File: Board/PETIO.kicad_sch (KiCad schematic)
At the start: 63 parts, among them CN2 PORT_CASSETTE_EDGE, CN3 PORT_IEEE_EDGE, IC11 74138N, IC12 74145N, IC15 VIA, IC17 PIA, IC20 PIA, IC21 7417N, IC22 7400N, IC23 7486N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

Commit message: ultipet 1.1a board
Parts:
- removed R101, R34, R35, R86, R87: 4k7, cbm_ultipet_v1:0207_10, symbol cbm_ultipet_v1-eagle-import:R-EU_0207/10
- added IC48: 7414N, cbm_ultipet_v1:DIL14, symbol cbm_ultipet_v1-eagle-import:7414N
- added RN7: 4k7, cbm_ultipet_v1:RN-8, symbol cbm_ultipet_v1-eagle-import:RN07
- RN3, RN5: value 5k1 -> 2k4
- RN4, RN6: value 2k4 -> 5k1
- T6, T7: footprint cbm_ultipet_v1:TO92 -> Package_TO_SOT_THT:TO-92L_Inline_Wide
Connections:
- net BA2: now also IC48.1 (I)
- net C1MTR: now also RN7.3
- net C2MTR: now also RN7.4
- net OPENHIGH: now also RN7.2
- net VCC: now also RN7.1; no longer IC17.22 (CS0), IC20.22 (CS0)
- net VDRIVE: now also RN7.6
- net /SEL0: now reaches IC9.15 (Y0)
- net /SEL2 renamed /SEL2
- new net FUC1: RN7.5
- new net PULLUP_UART: RN7.7
- new net /BA2: IC17.22 (CS0), IC20.22 (CS0), IC48.2 (O)
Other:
- note added: "$e810-$e813"
- note added: "$e820-$e823"
- note added: "1.0B: - fix IEEE488 pull up/down resistor values (again) 1.1A: - fully decode PIA addresses - replace some discrete Rs with RN7 - fix 2N2222 footprint for new BOM part"
- note added: "CBM-ULTIPET-V1.1A"
- note added: "CBM-ULTIPET-V1.1A-20240616"
- note added: "To Pullups"
- note removed: "$e810-$e817 (2x)"
- note removed: "$e82x (4x)"
- note removed: "CBM-ULTIPET-V1.0A"
- note removed: "CBM-ULTIPET-V1.0A-20240104"
- moved on the sheet: RN3, RN5

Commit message: diverse fixes
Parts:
- removed JP15: JP1E, cbm_ultipet_v1:JP1, symbol cbm_ultipet_v1-eagle-import:JP1E
- removed JP8: JP2E, cbm_ultipet_v1:JP2, symbol cbm_ultipet_v1-eagle-import:JP2E
- added JP21: SolderJumper_3_Bridged12, Jumper:SolderJumper-3_P1.3mm_Bridged12_RoundedPad1.0x1.5mm_NumberLabels, symbol Jumper:SolderJumper_3_Bridged12
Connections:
- net BA7: now also IC9.4 (G2A); no longer IC11.4 (G2A)
- net GND: now also IC11.4 (G2A); no longer IC9.4 (G2A)
- net /LOCALIO: now also JP21.2 (C)
- net at IC11.15 (Y0): now also JP21.1 (A)
- net at IC11.7 (Y7): now also JP21.3 (B)
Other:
- note added: "1.0B: - fix IEEE488 pull up/down resistor values (again) 1.1A: - fully decode PIA addresses - replace some discrete Rs with RN7 - fix 2N2222 footprint for new BOM part 1.2A: - fix addressing 2nd SID by moving BA7 to IC9 - replace JP8 with a solder jumper (I/O block address)"
- note added: "CBM-ULTIPET-V1.2A"
- note added: "CBM-ULTIPET-V1.2A-20241010"
- note removed: "1.0B: - fix IEEE488 pull up/down resistor values (again) 1.1A: - fully decode PIA addresses - replace some discrete Rs with RN7 - fix 2N2222 footprint for new BOM part"
- note removed: "CBM-ULTIPET-V1.1A"
- note removed: "CBM-ULTIPET-V1.1A-20240616"

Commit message: various fixes as documented in github issues
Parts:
- D10: value 1N4148 -> 1N4448
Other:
- note added: "1.0B: - fix IEEE488 pull up/down resistor values (again) 1.1A: - fully decode PIA addresses - replace some discrete Rs with RN7 - fix 2N2222 footprint for new BOM part 1.2A: - fix addressing 2nd SID by moving BA7 to IC9 - replace JP8 with a solder jumper (I/O block address) - replace 1N4148 with 1N4448 for lower fwd voltage drop"
- note added: "CBM-ULTIPET-V1.2A-20241013"
- note removed: "1.0B: - fix IEEE488 pull up/down resistor values (again) 1.1A: - fully decode PIA addresses - replace some discrete Rs with RN7 - fix 2N2222 footprint for new BOM part 1.2A: - fix addressing 2nd SID by moving BA7 to IC9 - replace JP8 with a solder jumper (I/O block address)"
- note removed: "CBM-ULTIPET-V1.2A-20241010"
- moved on the sheet: D10
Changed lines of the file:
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@@
 	(wire
 		(pts
-			(xy 248.92 149.86) (xy 256.54 149.86)
+			(xy 248.92 153.67) (xy 256.54 153.67)
 		)
 		(stroke
@@
 	(wire
 		(pts
-			(xy 248.92 104.14) (xy 248.92 149.86)
+			(xy 248.92 104.14) (xy 248.92 153.67)
 		)
 		(stroke
@@
 	(wire
 		(pts
-			(xy 256.54 149.86) (xy 256.54 152.4)
+			(xy 256.54 153.67) (xy 256.54 157.48)
 		)
 		(stroke
@@
 	(wire
 		(pts
-			(xy 256.54 157.48) (xy 256.54 167.64)
+			(xy 256.54 162.56) (xy 256.54 167.64)
 		)
 		(stroke
@@
 		)
 	)
-	(text "1.0B: \n- fix IEEE488 pull up/down resistor values (again)\n1.1A:\n- fully decode PIA addresses\n- replace some discrete Rs with RN7\n- fix 2N2222 footprint for new BOM part\n1.2A:\n- fix addressing 2nd SID by moving BA7 to IC9\n- replace JP8 with a solder jumper (I/O block address)"
+	(text "1.0B: \n- fix IEEE488 pull up/down resistor values (again)\n1.1A:\n- fully decode PIA addresses\n- replace some discrete Rs with RN7\n- fix 2N2222 footprint for new BOM part\n1.2A:\n- fix addressing 2nd SID by moving BA7 to IC9\n- replace JP8 with a solder jumper (I/O block address)\n- replace 1N4148 with 1N4448 for lower fwd voltage drop"
 		(exclude_from_sim no)
-		(at 322.58 354.33 0)
+		(at 314.706 351.536 0)
 		(effects
 			(font
@@
 		)
 	)
-	(text "CBM-ULTIPET-V1.2A-20241010"
+	(text "CBM-ULTIPET-V1.2A-20241013\n"
 		(exclude_from_sim no)
 		(at 464.82 363.22 0)
@@
 	(global_label "/BIRQ"
 		(shape bidirectional)
-		(at 254 149.86 0)
+		(at 254 153.67 0)
 		(fields_autoplaced yes)
 		(effects
@@
 		)
 		(property "Intersheetrefs" "${INTERSHEET_REFS}"
-			(at 263.7039 149.86 0)
+			(at 263.7039 153.67 0)
 			(effects
 				(font
@@
 	(symbol
 		(lib_id "cbm_ultipet_v1-eagle-import:DIODE-D-5")
-		(at 256.54 154.94 270)
+		(at 256.54 160.02 270)
 		(unit 1)
 		(exclude_from_sim no)
@@
 		(dnp no)
 		(property "Reference" "D10"
-			(at 257.0226 157.48 0)
+			(at 257.0226 162.56 0)
 			(effects
 				(font
@@
 			)
 		)
-		(property "Value" "1N4148"
-			(at 254.2286 157.48 0)
+		(property "Value" "1N4448"
+			(at 254.2286 162.56 0)
 			(effects
 				(font
@@
 		)
 		(property "Footprint" "cbm_ultipet_v1:D-5"
-			(at 256.54 154.94 0)
+			(at 256.54 160.02 0)
 			(effects
 				(font
@@
 		)
 		(property "Datasheet" ""
-			(at 256.54 154.94 0)
+			(at 256.54 160.02 0)
 			(effects
 				(font
@@
 		)
 		(property "Description" ""
-			(at 256.54 154.94 0)
+			(at 256.54 160.02 0)
 			(effects
 				(font

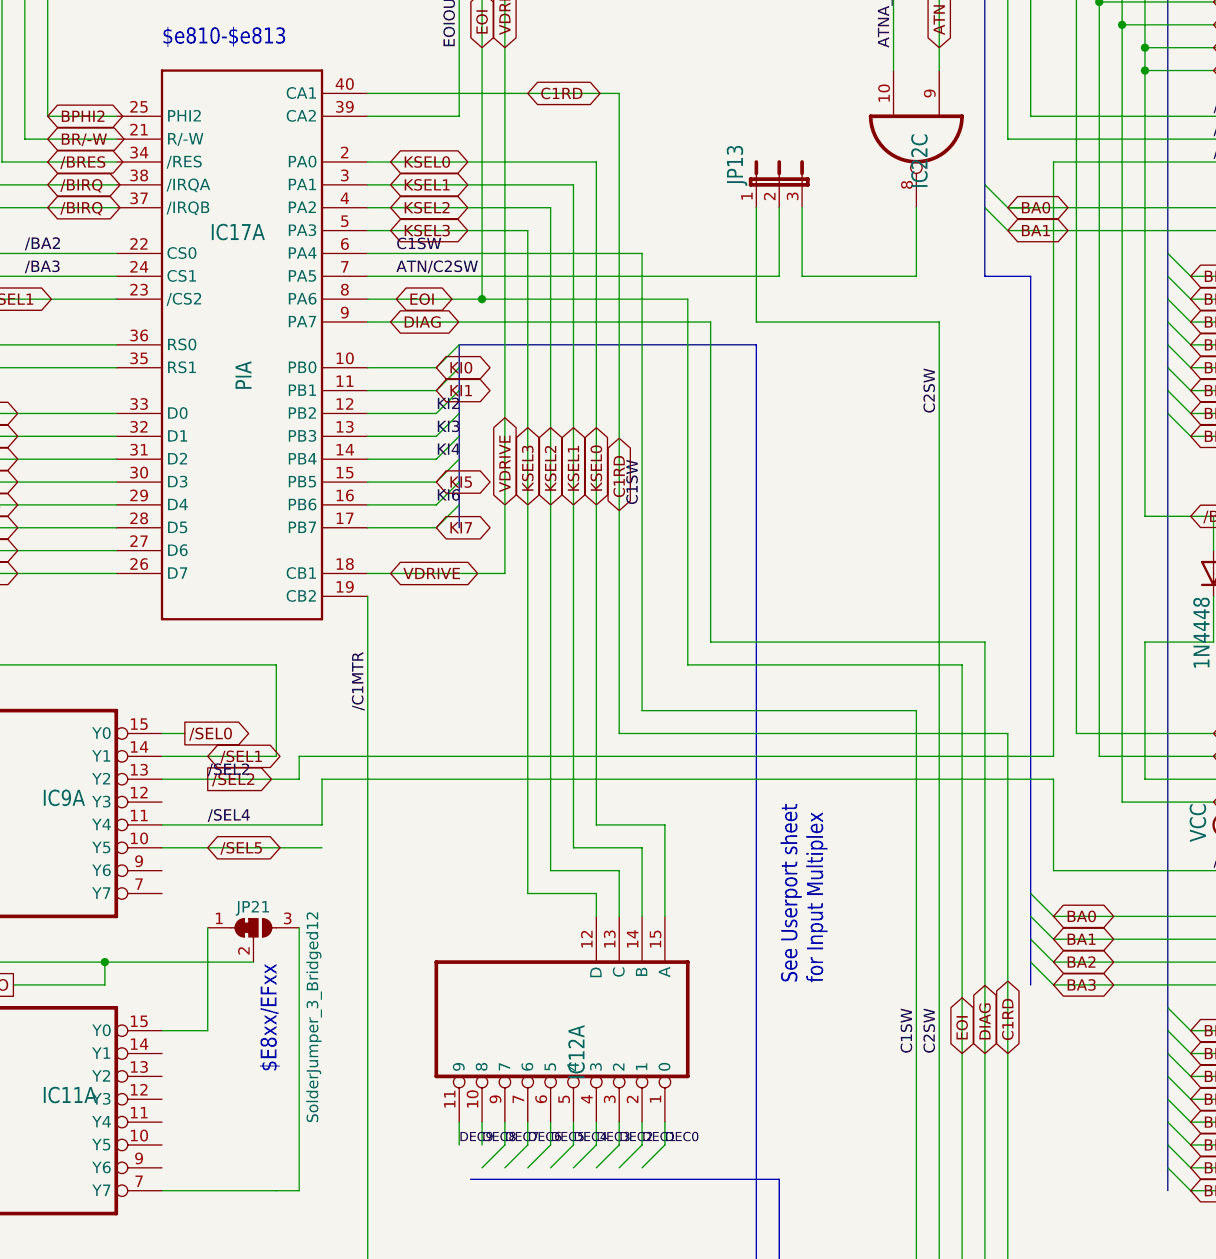
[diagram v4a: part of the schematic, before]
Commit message: replace some ultipet specific TQFP with easier to solder parts
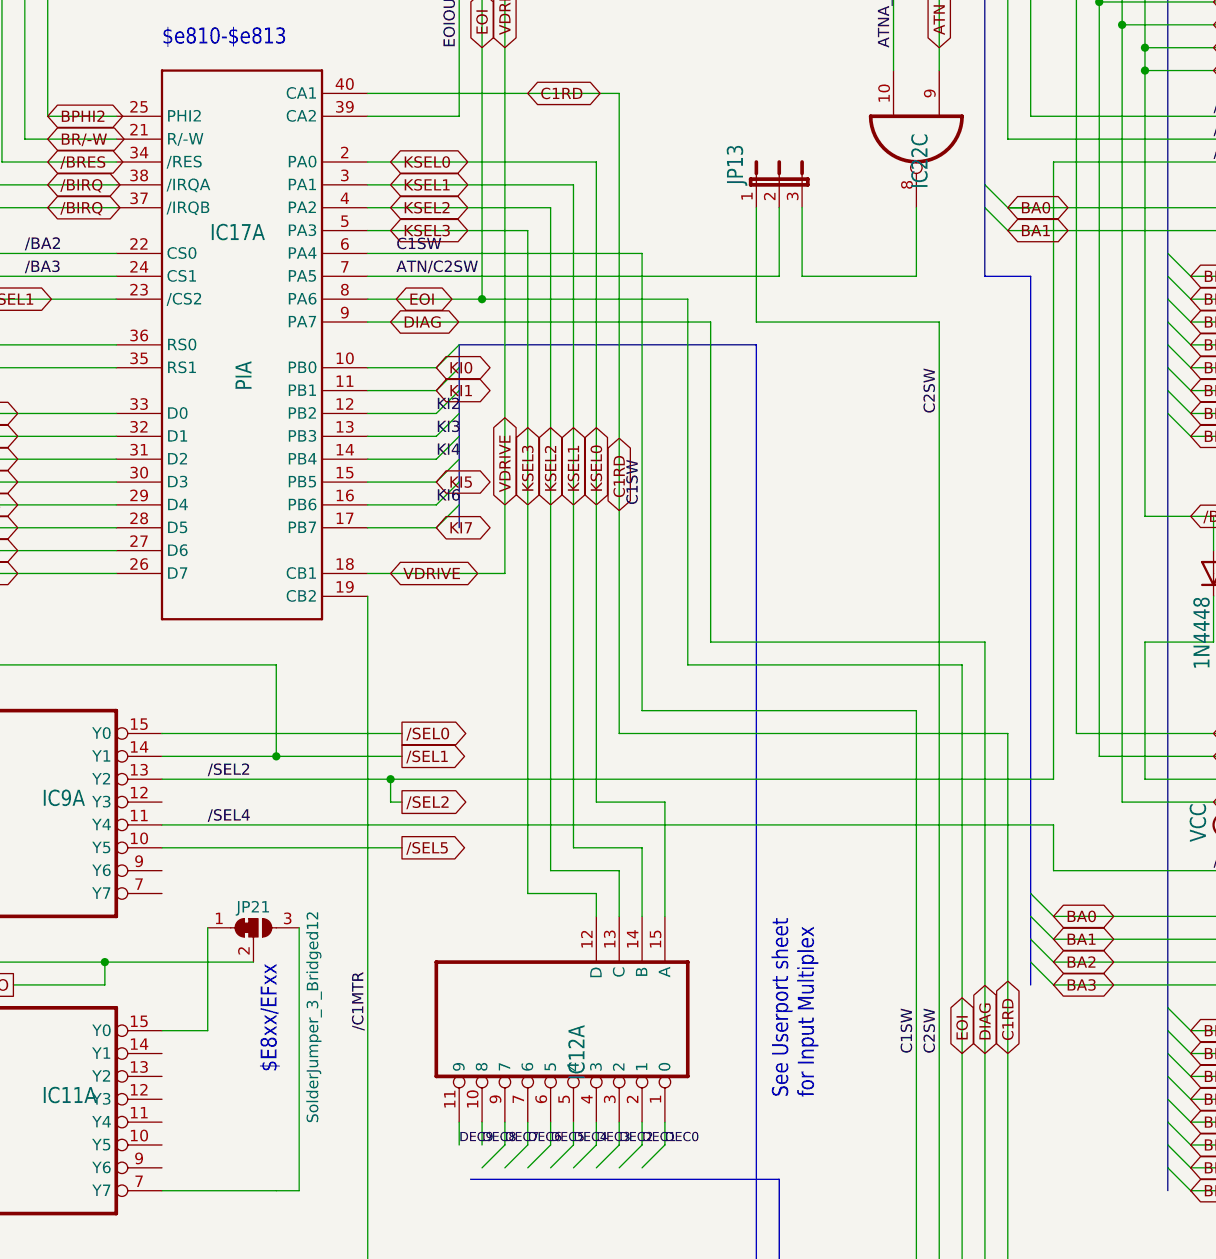
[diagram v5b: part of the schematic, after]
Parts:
- T6, T7: footprint Package_TO_SOT_THT:TO-92L_Inline_Wide -> cbm_ultipet_v1:TO92
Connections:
- net /SEL5 renamed /SEL5
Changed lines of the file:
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@@
 	)
 	(junction
+		(at 152.4 180.34)
+		(diameter 0)
+		(color 0 0 0 0)
+	)
+	(junction
 		(at 109.22 83.82)
 		(diameter 0)
@@
 	)
 	(junction
+		(at 165.1 182.88)
+		(diameter 0)
+		(color 0 0 0 0)
+	)
+	(junction
 		(at 461.01 208.28)
 		(diameter 0)
@@
 	(wire
 		(pts
-			(xy 195.58 187.96) (xy 187.96 187.96)
-		)
-		(stroke
-			(width 0.1524)
-			(type solid)
-		)
-	)
-	(wire
-		(pts
 			(xy 73.66 307.34) (xy 78.74 307.34)
 		)
@@
 	(wire
 		(pts
+			(xy 187.96 114.3) (xy 187.96 185.42)
+		)
+		(stroke
+			(width 0)
+			(type default)
+		)
+	)
+	(wire
+		(pts
 			(xy 162.56 370.84) (xy 162.56 365.76)
 		)
@@
 	(wire
 		(pts
+			(xy 139.7 187.96) (xy 238.76 187.96)
+		)
+		(stroke
+			(width 0.1524)
+			(type solid)
+		)
+	)
+	(wire
+		(pts
 			(xy 205.74 281.94) (xy 205.74 271.78)
 		)
@@
 	(wire
 		(pts
-			(xy 154.94 180.34) (xy 238.76 180.34)
-		)
-		(stroke
-			(width 0.1524)
-			(type solid)
-		)
-	)
-	(wire
-		(pts
 			(xy 162.56 149.86) (xy 170.18 149.86)
 		)
@@
 	(wire
 		(pts
-			(xy 157.48 182.88) (xy 238.76 182.88)
-		)
-		(stroke
-			(width 0.1524)
-			(type solid)
-		)
-	)
-	(wire
-		(pts
 			(xy 99.06 203.2) (xy 99.06 180.34)
 		)
@@
 	(wire
 		(pts
-			(xy 139.7 182.88) (xy 154.94 182.88)
+			(xy 139.7 182.88) (xy 165.1 182.88)
 		)
 		(stroke
@@
 	(wire
 		(pts
-			(xy 139.7 177.8) (xy 142.24 177.8)
+			(xy 139.7 177.8) (xy 166.37 177.8)
 		)
 		(stroke
@@
 	(wire
 		(pts
-			(xy 152.4 180.34) (xy 152.4 170.18)
+			(xy 226.06 81.28) (xy 226.06 104.14)
 		)
 		(stroke
@@
 	(wire
 		(pts
-			(xy 226.06 81.28) (xy 226.06 104.14)
+			(xy 162.56 139.7) (xy 170.18 139.7)
 		)
 		(stroke
@@
 	(wire
 		(pts
-			(xy 162.56 139.7) (xy 170.18 139.7)
+			(xy 154.94 199.39) (xy 154.94 228.6)
 		)
 		(stroke
-			(width 0.1524)
-			(type solid)
+			(width 0)
+			(type default)
 		)
 	)
 	(wire
 		(pts
-			(xy 154.94 199.39) (xy 154.94 228.6)
+			(xy 166.37 180.34) (xy 152.4 180.34)
 		)
 		(stroke
-			(width 0)
-			(type default)
+			(width 0.1524)
+			(type solid)
 		)
 	)
@@
 	(wire
 		(pts
-			(xy 139.7 190.5) (xy 157.48 190.5)
+			(xy 139.7 190.5) (xy 166.37 190.5)
 		)
 		(stroke
@@
 	(wire
 		(pts
-			(xy 195.58 198.12) (xy 195.58 187.96)
-		)
-		(stroke
-			(width 0.1524)
-			(type solid)
-		)
-	)
-	(wire
-		(pts
 			(xy 121.92 114.3) (xy 121.92 73.66)
 		)
@@
 	(wire
 		(pts
-			(xy 162.56 114.3) (xy 187.96 114.3)
-		)
-		(stroke
-			(width 0.1524)
-			(type solid)
-		)
-	)
-	(wire
-		(pts
 			(xy 297.18 256.54) (xy 299.72 256.54)
 		)
@@
 	(wire
 		(pts
+			(xy 162.56 114.3) (xy 187.96 114.3)
+		)
+		(stroke
+			(width 0)
+			(type default)
+		)
+	)
+	(wire
+		(pts
 			(xy 170.18 363.22) (xy 180.34 363.22)
 		)
@@
 	(wire
 		(pts
-			(xy 238.76 114.3) (xy 238.76 180.34)
+			(xy 238.76 114.3) (xy 238.76 182.88)
 		)
 		(stroke
@@
 	(wire
 		(pts
+			(xy 165.1 182.88) (xy 238.76 182.88)
+		)
+		(stroke
+			(width 0.1524)
+			(type solid)
+		)
+	)
+	(wire
+		(pts
 			(xy 345.44 264.16) (xy 365.76 264.16)
 		)
@@
 	(wire
 		(pts
-			(xy 157.48 187.96) (xy 157.48 182.88)
-		)
-		(stroke
-			(width 0.1524)
-			(type solid)
-		)
-	)
-	(wire
-		(pts
 			(xy 447.04 54.61) (xy 447.04 63.5)
 		)
@@
 	(wire
 		(pts
+			(xy 195.58 185.42) (xy 195.58 198.12)
+		)
+		(stroke
+			(width 0)
+			(type default)
+		)
+	)
+	(wire
+		(pts
 			(xy 424.18 154.94) (xy 330.2 154.94)
 		)
@@
 	(wire
 		(pts
-			(xy 139.7 187.96) (xy 157.48 187.96)
-		)
-		(stroke
-			(width 0.1524)
-			(type solid)
-		)
-	)
-	(wire
-		(pts
 			(xy 495.3 99.06) (xy 495.3 88.9)
 		)
@@
 		)
 	)
+	(wire
+		(pts
+			(xy 165.1 185.42) (xy 165.1 182.88)
+		)
+		(stroke
+			(width 0.1524)
+			(type solid)
+		)
+	)
 	(bus
 		(pts
@@
 	(wire
 		(pts
+			(xy 187.96 185.42) (xy 195.58 185.42)
+		)
+		(stroke
+			(width 0)
+			(type default)
+		)
+	)
+	(wire
+		(pts
 			(xy 43.18 101.6) (xy 43.18 106.68)
 		)
@@
 	(wire
 		(pts
-			(xy 238.76 182.88) (xy 238.76 193.04)
+			(xy 238.76 187.96) (xy 238.76 193.04)
 		)
 		(stroke
@@
 	(wire
 		(pts
-			(xy 154.94 182.88) (xy 154.94 180.34)
+			(xy 297.18 292.1) (xy 320.04 292.1)
 		)
 		(stroke
@@
 	(wire
 		(pts
-			(xy 297.18 292.1) (xy 320.04 292.1)
+			(xy 461.01 203.2) (xy 462.28 203.2)
 		)
 		(stroke
-			(width 0.1524)
-			(type solid)
+			(width 0)
+			(type default)
 		)
 	)
 	(wire
 		(pts
-			(xy 461.01 203.2) (xy 462.28 203.2)
+			(xy 165.1 185.42) (xy 166.37 185.42)
 		)
 		(stroke
-			(width 0)
-			(type default)
+			(width 0.1524)
+			(type solid)
 		)
 	)
@@
 	(wire
 		(pts
+			(xy 162.56 162.56) (xy 162.56 259.08)
+		)
+		(stroke
+			(width 0.1524)
+			(type solid)
+		)
+	)
+	(wire
+		(pts
 			(xy 543.56 287.02) (xy 543.56 292.1)
 		)
@@
 	(wire
 		(pts
-			(xy 187.96 187.96) (xy 187.96 114.3)
-		)
-		(stroke
-			(width 0.1524)
-			(type solid)
-		)
-	)
-	(wire
-		(pts
 			(xy 45.72 271.78) (xy 53.34 271.78)
 		)
@@
 	(wire
 		(pts
-			(xy 162.56 162.56) (xy 162.56 259.08)
-		)
-		(stroke
-			(width 0.1524)
-			(type solid)
-		)
-	)
-	(wire
-		(pts
 			(xy 314.96 91.44) (xy 314.96 81.28)
 		)
@@
 	(wire
 		(pts
+			(xy 152.4 170.18) (xy 152.4 180.34)
+		)
+		(stroke
+			(width 0.1524)
+			(type solid)
+		)
+	)
+	(wire
+		(pts
 			(xy 55.88 182.88) (xy 83.82 182.88)
 		)
@@
 	(text "See Userport sheet\nfor Input Multiplex"
 		(exclude_from_sim no)
-		(at 213.36 205.74 90)
+		(at 212.344 218.44 90)
 		(effects
 			(font
@@
 	)
 	(label "/C1MTR"
-		(at 162.56 175.26 90)
+		(at 162.56 210.82 90)
 		(fields_autoplaced yes)
 		(effects
@@
 	(global_label "{slash}SEL2"
 		(shape output)
-		(at 144.78 182.88 0)
+		(at 166.37 185.42 0)
 		(fields_autoplaced yes)
 		(effects
@@
 		)
 		(property "Intersheetrefs" "${INTERSHEET_REFS}"
-			(at 153.6918 182.88 0)
+			(at 175.2818 185.42 0)
 			(effects
 				(font
@@
 		)
 	)
-	(global_label "/SEL1"
-		(shape bidirectional)
-		(at 144.78 180.34 0)
+	(global_label "{slash}SEL1"
+		(shape output)
+		(at 166.37 180.34 0)
 		(fields_autoplaced yes)
 		(effects
@@
 		)
 		(property "Intersheetrefs" "${INTERSHEET_REFS}"
-			(at 154.6023 180.34 0)
+			(at 175.1033 180.34 0)
 			(effects
 				(font
@@
 		)
 	)
-	(global_label "/SEL5"
-		(shape bidirectional)
-		(at 144.78 190.5 0)
+	(global_label "{slash}SEL5"
+		(shape output)
+		(at 166.37 190.5 0)
 		(fields_autoplaced yes)
 		(effects
@@
 		)
 		(property "Intersheetrefs" "${INTERSHEET_REFS}"
-			(at 154.6023 190.5 0)
+			(at 175.1033 190.5 0)
 			(effects
 				(font
@@
 	(global_label "{slash}SEL0"
 		(shape output)
-		(at 142.24 177.8 0)
+		(at 166.37 177.8 0)
 		(fields_autoplaced yes)
 		(effects
@@
 		)
 		(property "Intersheetrefs" "${INTERSHEET_REFS}"
-			(at 151.1518 177.8 0)
+			(at 175.2818 177.8 0)
 			(effects
 				(font
@@
 			)
 		)
-		(property "Footprint" "Package_TO_SOT_THT:TO-92L_Inline_Wide"
+		(property "Footprint" "cbm_ultipet_v1:TO92"
 			(at 152.4 360.68 0)
 			(effects
@@
 			)
 		)
-		(property "Footprint" "Package_TO_SOT_THT:TO-92L_Inline_Wide"
+		(property "Footprint" "cbm_ultipet_v1:TO92"
 			(at 182.88 363.22 0)
 			(effects

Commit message: work on 1.3
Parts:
- IC11, IC12, IC9: footprint cbm_ultipet_v1:DIL16 -> Package_DIP:DIP-16_W7.62mm_Socket_LongPads
- IC15, IC17, IC20: footprint cbm_ultipet_v1:DIL40 -> Package_DIP:DIP-42_W15.24mm_Socket_LongPads
- IC21, IC22, IC23, IC48: footprint cbm_ultipet_v1:DIL14 -> Package_DIP:DIP-14_W7.62mm_Socket_LongPads
- U$20, U$21: footprint cbm_ultipet_v1:DIL20 -> Package_DIP:DIP-20_W7.62mm_Socket_LongPads

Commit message: more work on r1.3
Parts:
- removed P8: PETKEYBD, cbm_ultipet_v1:C64KEYB, symbol cbm_ultipet_v1-eagle-import:PETKEYBD
- added J14: Extended_PET_keyboard_connector, cbm_ultipet_v1:PET_Extended_Keyboard_Connector, symbol petkn:Extended_PET_keyboard_connector
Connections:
- net DEC0: now also J14.12
- net DEC1: now also J14.11
- net DEC2: now also J14.10
- net DEC3: now also J14.9
- net DEC4: now also J14.8
- net DEC5: now also J14.7
- net DEC6: now also J14.6
- net DEC7: now also J14.5
- net DEC8: now also J14.4
- net DEC9: now also J14.3
- net GND: now also J14.1, J14.21 (GND)
- net KI0: now also J14.20
- net KI1: now also J14.19
- net KI2: now also J14.18
- net KI3: now also J14.17
- net KI4: now also J14.16
- net KI5: now also J14.15
- net KI6: now also J14.14
- net KI7: now also J14.13
- net KSEL0: now also J14.22 (S0)
- net KSEL1: now also J14.23 (S1)
- net KSEL2: now also J14.24 (S2)
- net KSEL3: now also J14.25 (S3)
- net VCC: now also J14.26 (VCC5)
- net at P2.3 (RSTR): now also J14.30 (RESTORE)
- new net SCA: J14.29 (SCA)
- new net SCL: J14.28 (SCL)
- new net V33: J14.27 (VCC33)
